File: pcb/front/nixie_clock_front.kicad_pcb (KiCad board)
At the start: 2 copper layers, 110 x 50 mm, 22 parts, among them J1 Conn_01x10_Male, J2 Conn_01x10_Male, U1 74141, U2 74141, U3 74141, U4 74141

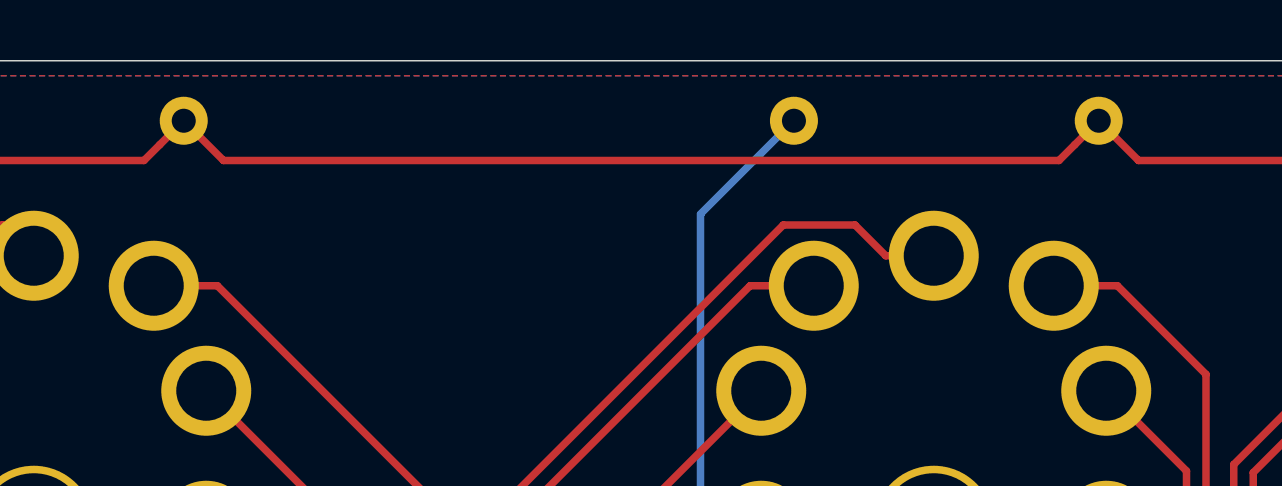
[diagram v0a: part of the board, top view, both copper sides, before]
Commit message: Back panel PCB
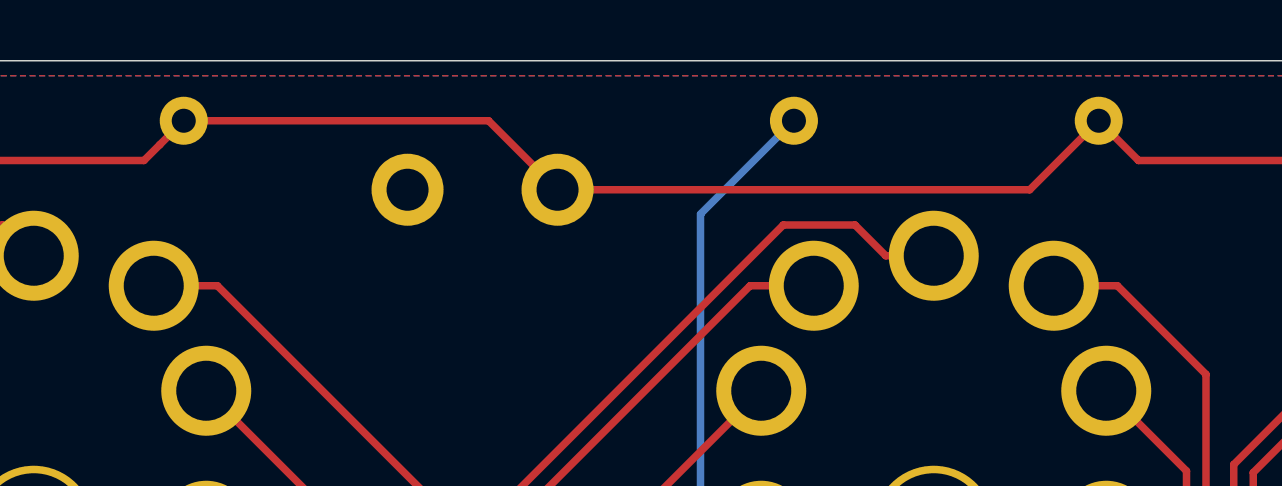
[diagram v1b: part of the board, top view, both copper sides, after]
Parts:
- added J3: HV_IN, nixie_clock:Terminal_Block_KF301-5.0-2P, B.Cu at (107.5, 54.3)
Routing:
- net VDD: track 95.2 -> 96.0 mm
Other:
- board text added: "+"
- board text added: "⏚"
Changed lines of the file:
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@@
   (general
     (thickness 1.6)
-    (drawings 7)
+    (drawings 12)
     (tracks 362)
     (zones 0)
-    (modules 22)
+    (modules 23)
     (nets 64)
   )
@@
       (rotate (xyz 0 0 0))
     )
+  )
+  (module nixie_clock:Terminal_Block_KF301-5.0-2P (layer B.Cu)
+    (at 107.46 54.3 180)
+    (fp_text reference J3 (at 0 -7) (layer B.SilkS) hide
+      (effects (font (size 1 1) (thickness 0.15)) (justify mirror))
+    )
+    (fp_text value HV_IN (at 2.37 -4.85) (layer B.SilkS)
+      (effects (font (size 1 1) (thickness 0.15)) (justify mirror))
+    )
+    (fp_line (start -2.5 -3.5) (end 7.5 -3.5) (layer B.SilkS) (width 0.1))
+    (fp_line (start 7.5 -3.5) (end 7.5 4) (layer B.SilkS) (width 0.1))
+    (fp_line (start 7.5 4) (end -2.5 4) (layer B.SilkS) (width 0.1))
+    (fp_line (start -2.5 4) (end -2.5 -3.5) (layer B.SilkS) (width 0.1))
+    (fp_line (start -2.5 4) (end 7.5 4) (layer B.CrtYd) (width 0.12))
+    (fp_line (start 7.5 4) (end 7.5 -3.5) (layer B.CrtYd) (width 0.12))
+    (fp_line (start 7.5 -3.5) (end -2.5 -3.5) (layer B.CrtYd) (width 0.12))
+    (fp_line (start -2.5 -3.5) (end -2.5 4) (layer B.CrtYd) (width 0.12))
+    (fp_line (start -1.25 4) (end -1.25 2.75) (layer B.SilkS) (width 0.1))
+    (fp_line (start -1.25 2.75) (end 1.25 2.75) (layer B.SilkS) (width 0.1))
+    (fp_line (start 1.25 2.75) (end 1.25 4) (layer B.SilkS) (width 0.1))
+    (fp_line (start 3.75 4) (end 3.75 2.75) (layer B.SilkS) (width 0.1))
+    (fp_line (start 3.75 2.75) (end 6.25 2.75) (layer B.SilkS) (width 0.1))
+    (fp_line (start 6.25 2.75) (end 6.25 4) (layer B.SilkS) (width 0.1))
+    (pad 1 thru_hole circle (at 0 0 180) (size 2.4 2.4) (drill 1.4) (layers *.Cu *.Mask)
+      (net 19 VDD))
+    (pad 2 thru_hole circle (at 5 0 180) (size 2.4 2.4) (drill 1.4) (layers *.Cu *.Mask)
+      (net 2 GND))
+  )
+  (gr_text ⏚ (at 98.59 54.42) (layer B.SilkS)
+    (effects (font (size 1.5 1.5) (thickness 0.3)) (justify mirror))
+  )
+  (gr_text + (at 111.16 54.3) (layer B.SilkS)
+    (effects (font (size 1.5 1.5) (thickness 0.3)) (justify mirror))
+  )
+  (dimension 13.500093 (width 0.15) (layer Dwgs.User)
+    (gr_text "13.500 mm" (at 45.725263 56.773147 -89.78779438) (layer Dwgs.User)
+      (effects (font (size 1 1) (thickness 0.15)))
+    )
+    (feature1 (pts (xy 51.95 50) (xy 46.413837 50.020504)))
+    (feature2 (pts (xy 52 63.5) (xy 46.463837 63.520504)))
+    (crossbar (pts (xy 47.050254 63.518332) (xy 47.000254 50.018332)))
+    (arrow1a (pts (xy 47.000254 50.018332) (xy 47.590843 51.142656)))
+    (arrow1b (pts (xy 47.000254 50.018332) (xy 46.418009 51.147)))
+    (arrow2a (pts (xy 47.050254 63.518332) (xy 47.632499 62.389664)))
+    (arrow2b (pts (xy 47.050254 63.518332) (xy 46.459665 62.394008)))
+  )
+  (dimension 50 (width 0.15) (layer Dwgs.User)
+    (gr_text "50.000 mm" (at 164.1 75 90) (layer Dwgs.User)
+      (effects (font (size 1 1) (thickness 0.15)))
+    )
+    (feature1 (pts (xy 160 50) (xy 163.386421 50)))
+    (feature2 (pts (xy 160 100) (xy 163.386421 100)))
+    (crossbar (pts (xy 162.8 100) (xy 162.8 50)))
+    (arrow1a (pts (xy 162.8 50) (xy 163.386421 51.126504)))
+    (arrow1b (pts (xy 162.8 50) (xy 162.213579 51.126504)))
+    (arrow2a (pts (xy 162.8 100) (xy 163.386421 98.873496)))
+    (arrow2b (pts (xy 162.8 100) (xy 162.213579 98.873496)))
+  )
+  (dimension 110 (width 0.15) (layer Dwgs.User)
+    (gr_text "110.000 mm" (at 105 45.2) (layer Dwgs.User)
+      (effects (font (size 1 1) (thickness 0.15)))
+    )
+    (feature1 (pts (xy 50 50) (xy 50 45.913579)))
+    (feature2 (pts (xy 160 50) (xy 160 45.913579)))
+    (crossbar (pts (xy 160 46.5) (xy 50 46.5)))
+    (arrow1a (pts (xy 50 46.5) (xy 51.126504 45.913579)))
+    (arrow1b (pts (xy 50 46.5) (xy 51.126504 47.086421)))
+    (arrow2a (pts (xy 160 46.5) (xy 158.873496 45.913579)))
+    (arrow2b (pts (xy 160 46.5) (xy 158.873496 47.086421)))
   )
   (gr_text "Nixie Clock Front Panel v2 by Ilya Strukov" (at 104.95 79.35) (layer B.SilkS)
@@
   (segment (start 73.325001 53.325001) (end 93.674999 53.325001) (width 0.25) (layer F.Cu) (net 19))
   (segment (start 72 52) (end 73.325001 53.325001) (width 0.25) (layer F.Cu) (net 19))
-  (segment (start 124.700001 52.799999) (end 125.5 52) (width 0.25) (layer F.Cu) (net 19))
-  (segment (start 124.174999 53.325001) (end 124.700001 52.799999) (width 0.25) (layer F.Cu) (net 19))
-  (segment (start 96.325001 53.325001) (end 124.174999 53.325001) (width 0.25) (layer F.Cu) (net 19))
-  (segment (start 95 52) (end 96.325001 53.325001) (width 0.25) (layer F.Cu) (net 19))
   (segment (start 158 61.55) (end 158 63.5) (width 0.25) (layer F.Cu) (net 19))
   (segment (start 148.45 52) (end 158 61.55) (width 0.25) (layer F.Cu) (net 19))
@@
   (segment (start 146.674999 53.325001) (end 147.200001 52.799999) (width 0.25) (layer F.Cu) (net 19))
   (segment (start 125.5 52) (end 126.825001 53.325001) (width 0.25) (layer F.Cu) (net 19))
+  (segment (start 123.2 54.3) (end 125.5 52) (width 0.25) (layer F.Cu) (net 19))
+  (segment (start 107.46 54.3) (end 123.2 54.3) (width 0.25) (layer F.Cu) (net 19))
+  (segment (start 105.16 52) (end 107.46 54.3) (width 0.25) (layer F.Cu) (net 19))
+  (segment (start 95 52) (end 105.16 52) (width 0.25) (layer F.Cu) (net 19))
   (segment (start 108 90.7) (end 108 91.75) (width 0.25) (layer F.Cu) (net 20))
   (segment (start 106.024989 64.434439) (end 106.024989 88.724989) (width 0.25) (layer F.Cu) (net 20))
